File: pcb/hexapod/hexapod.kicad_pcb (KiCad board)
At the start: 2 copper layers, 48 x 110 mm, 28 parts, among them J1 Conn_01x03, J10 Conn_01x03, J11 Conn_01x03, J12 Conn_01x03, J13 Conn_01x03, J14 Conn_01x03, J15 Conn_01x03, J16 Conn_01x03, J17 Conn_01x03, J18 Conn_01x03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

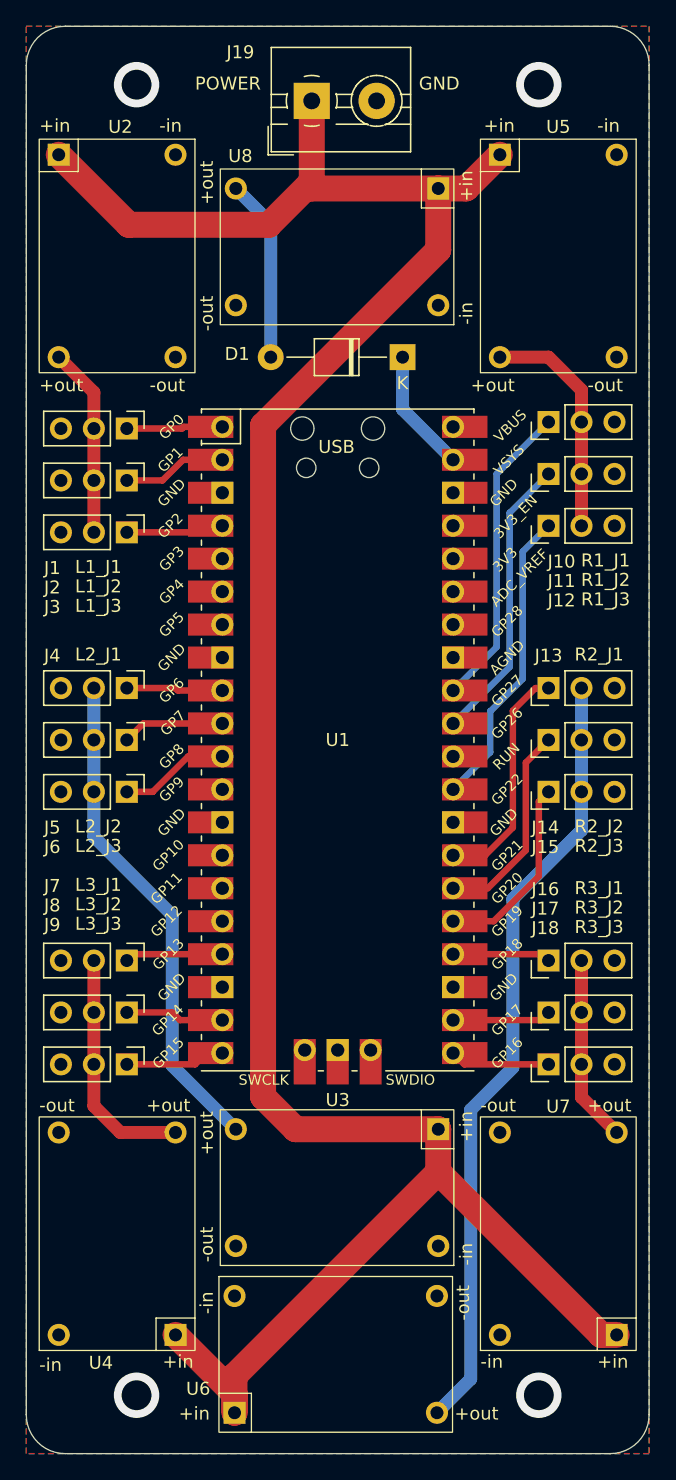
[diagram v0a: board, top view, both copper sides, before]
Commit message: update Mini360 pad
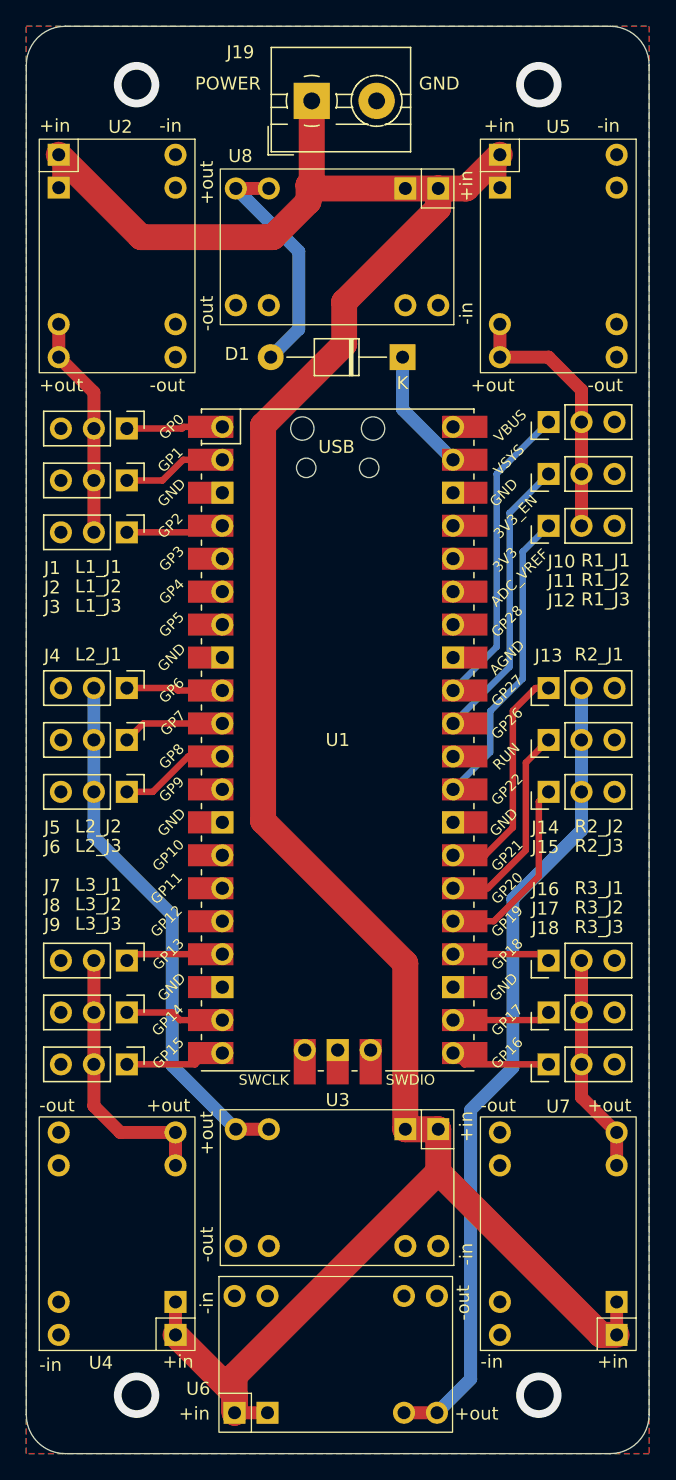
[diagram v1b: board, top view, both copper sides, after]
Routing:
- net /power: track 190.6 -> 199.9 mm
- net Net-(D1-A): track 14.1 -> 18.4 mm
- net /power_r2: track 60.5 -> 63.0 mm
- net /power_r1: track 17.8 -> 20.3 mm
- net /power_l1: track 14.6 -> 17.2 mm
- net /power_l3: track 18.3 -> 20.9 mm
- net /power_l2: track 38.5 -> 41.1 mm
- net /power_r3: track 14.4 -> 16.9 mm

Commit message: fix pcb
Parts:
- removed U3, U4, U6, U7: ~, Hexapod_Library:Mini360
- U2, U5: footprint Hexapod_Library:Mini360 -> Hexapod_Library:XL4005
- moved D1 54.3 mm to (105.1, 124.8)
- moved U8 35.2 mm to (105.9, 103.1), turned to -90 degrees
- moved J10 27.5 mm to (116.2, 103.0)
- moved J11 27.5 mm to (116.2, 107.0)
- moved J12 27.5 mm to (116.2, 111.0)
- moved J1 27.0 mm to (83.8, 103.0)
- moved J2 27.0 mm to (83.8, 107.0)
- moved J3 27.0 mm to (83.8, 111.0)
- moved U1 27.0 mm to (100.0, 127.0)
- moved J13 21.8 mm to (116.2, 117.8)
- moved J14 21.8 mm to (116.2, 121.8)
- moved J15 21.8 mm to (116.2, 125.8)
- moved J4 21.5 mm to (83.8, 117.5)
- moved J5 21.5 mm to (83.8, 121.5)
- moved J6 21.5 mm to (83.8, 125.5)
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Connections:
- J13 pad 2: /power_r2 -> /power_r1
- J14 pad 2: /power_r2 -> /power_r1
- J15 pad 2: /power_r2 -> /power_r1
- J16 pad 2: /power_r3 -> /power_r1
- J17 pad 2: /power_r3 -> /power_r1
- J18 pad 2: /power_r3 -> /power_r1
- J4 pad 2: /power_l2 -> /power_l1
- J5 pad 2: /power_l2 -> /power_l1
- J6 pad 2: /power_l2 -> /power_l1
- J7 pad 2: /power_l3 -> /power_l1
- J8 pad 2: /power_l3 -> /power_l1
- J9 pad 2: /power_l3 -> /power_l1
- U1 pad 10: /l2_j2 -> /l2_j3
- U1 pad 11: /l2_j3 -> unconnected-(U1-GPIO8-Pad11)
- U1 pad 12: unconnected-(U1-GPIO9-Pad12) -> /l3_j1
- U1 pad 16: unconnected-(U1-GPIO12-Pad16) -> /l3_j2
- U1 pad 17: /l3_j1 -> /l3_j3
- U1 pad 19: /l3_j2 -> unconnected-(U1-GPIO14-Pad19)
- U1 pad 20: /l3_j3 -> unconnected-(U1-GPIO15-Pad20)
- U1 pad 7: unconnected-(U1-GPIO5-Pad7) -> /l2_j1
- U1 pad 9: /l2_j1 -> /l2_j2
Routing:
- net /power: track 199.9 -> 86.8 mm
- net /power_r2: track 63.0 -> 0.00 mm
- net /power_l2: track 41.1 -> 0.00 mm
- net /power_r1: track 20.3 -> 58.0 mm
- net /power_l1: track 17.2 -> 44.9 mm
- net /power_l3: track 20.9 -> 0.00 mm
- net /power_r3: track 16.9 -> 0.00 mm
- net Net-(D1-K): track 9.52 -> 21.4 mm
- net Net-(D1-A): track 18.4 -> 7.59 mm
- net /r3_j2: track 7.60 -> 15.6 mm
- net /r3_j3: track 7.72 -> 15.3 mm
- net /r3_j1: track 7.56 -> 14.6 mm
- net /r2_j2: track 16.0 -> 20.9 mm
- net /r2_j3: track 14.9 -> 19.4 mm
- net /r2_j1: track 18.0 -> 21.2 mm
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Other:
- board text added: "+BATTERY"
- board text added: "Hexapod v2.0 (c) rookidroid.com Make Robotics Accessible and Fun for Everyone"
- board text removed: "Hexapod v2.1 (c) rookidroid.com Make Robotics Accessible and Fun for Everyone"
- board text removed: "POWER"
- board text removed: "USB"

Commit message: update
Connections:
- net Net-(D1-K) renamed /VSYS
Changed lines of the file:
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@@
 	(net 34 "/power")
 	(net 35 "/power_l1")
-	(net 36 "Net-(D1-K)")
+	(net 36 "/VSYS")
 	(net 37 "Net-(D1-A)")
 	(footprint "Connector_PinHeader_2.54mm:PinHeader_1x03_P2.54mm_Vertical"
@@
 			(layers "*.Cu" "*.Mask")
 			(remove_unused_layers no)
-			(net 36 "Net-(D1-K)")
+			(net 36 "/VSYS")
 			(pinfunction "K")
 			(pintype "passive")
@@
 		(tags "Through hole pin header THT 1x03 2.54mm single row")
 		(property "Reference" "J3"
-			(at -2 -1.5 360)
+			(at -2 -1.5 0)
 			(layer "F.SilkS")
 			(effects
@@
 		(tags "Through hole pin header THT 1x03 2.54mm single row")
 		(property "Reference" "J1"
-			(at -1.75 -2.25 360)
+			(at -1.75 -2.25 0)
 			(layer "F.SilkS")
 			(effects
@@
 		(tags "Through hole pin header THT 1x03 2.54mm single row")
 		(property "Reference" "J6"
-			(at -2 -1.5 360)
+			(at -2 -1.5 0)
 			(layer "F.SilkS")
 			(effects
@@
 		(tags "Through hole pin header THT 1x03 2.54mm single row")
 		(property "Reference" "J9"
-			(at -2 -1.5 360)
+			(at -2 -1.5 0)
 			(layer "F.SilkS")
 			(effects
@@
 		(tags "Through hole pin header THT 1x03 2.54mm single row")
 		(property "Reference" "J8"
-			(at -2 -1.5 360)
+			(at -2 -1.5 0)
 			(layer "F.SilkS")
 			(effects
@@
 		(tags "Through hole pin header THT 1x03 2.54mm single row")
 		(property "Reference" "J2"
-			(at -2 -1.5 360)
+			(at -2 -1.5 0)
 			(layer "F.SilkS")
 			(effects
@@
 			(layers "*.Cu" "*.Mask")
 			(remove_unused_layers no)
-			(net 36 "Net-(D1-K)")
+			(net 36 "/VSYS")
 			(pinfunction "VSYS")
 			(pintype "power_in")
@@
 			)
 			(layers "F.Cu" "F.Mask")
-			(net 36 "Net-(D1-K)")
+			(net 36 "/VSYS")
 			(pinfunction "VSYS")
 			(pintype "power_in")
@@
 		(tags "Through hole pin header THT 1x03 2.54mm single row")
 		(property "Reference" "J5"
-			(at -2 -1.75 360)
+			(at -2 -1.75 0)
 			(layer "F.SilkS")
 			(effects
@@
 		(tags "Through hole pin header THT 1x03 2.54mm single row")
 		(property "Reference" "J7"
-			(at -2 -1.5 360)
+			(at -2 -1.5 0)
 			(layer "F.SilkS")
 			(effects
@@
 		(fp_arc
 			(start 3.521125 1.286294)
-			(mid 3.477135 1.233898)
+			(mid 3.477135 1.233899)
 			(end 3.435 1.18)
 			(stroke
@@
 		(fp_arc
 			(start 3.521202 -1.287012)
-			(mid 3.578748 -1.350292)
+			(mid 3.578747 -1.350293)
 			(end 3.639 -1.411)
 			(stroke
@@
 		(fp_arc
 			(start 3.93363 -1.644317)
-			(mid 4.00637 -1.689264)
+			(mid 4.006369 -1.689267)
 			(end 4.081 -1.731)
 			(stroke
@@
 		(fp_arc
 			(start 4.080344 1.730739)
-			(mid 4.005725 1.688977)
+			(mid 4.005725 1.688978)
 			(end 3.933 1.644)
 			(stroke
@@
 		(fp_arc
 			(start 5.000479 1.960685)
-			(mid 4.744554 1.943974)
+			(mid 4.744554 1.943973)
 			(end 4.493 1.894)
 			(stroke
@@
 		(fp_arc
 			(start 5.638712 -1.85392)
-			(mid 5.734863 -1.817952)
+			(mid 5.734863 -1.817951)
 			(end 5.829 -1.777)
 			(stroke
@@
 		(fp_arc
 			(start 5.829295 1.77705)
-			(mid 5.735154 1.818015)
+			(mid 5.735155 1.818016)
 			(end 5.639 1.854)
 			(stroke
@@
 		(fp_arc
 			(start 5.920652 -1.730826)
-			(mid 5.995273 -1.68902)
+			(mid 5.995274 -1.689022)
 			(end 6.068 -1.644)
 			(stroke
@@
 		(fp_arc
 			(start 6.096479 -1.625751)
-			(mid 6.166349 -1.576376)
+			(mid 6.166348 -1.576374)
 			(end 6.234 -1.524)
 			(stroke
@@
 		(fp_arc
 			(start 6.233457 1.523294)
-			(mid 6.165839 1.575648)
+			(mid 6.16584 1.575649)
 			(end 6.096 1.625)
 			(stroke
@@
 		(fp_arc
 			(start 6.36213 1.410651)
-			(mid 6.299301 1.468722)
+			(mid 6.2993 1.468721)
 			(end 6.234 1.524)
 			(stroke
@@
 		(fp_arc
 			(start 6.566102 1.179628)
-			(mid 6.523978 1.233565)
+			(mid 6.523978 1.233564)
 			(end 6.48 1.286)
 			(stroke
